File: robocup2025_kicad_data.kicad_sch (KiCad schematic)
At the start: 15 parts, among them M7 Motor_Servo, U2 ESP32-DEVKITC-32E

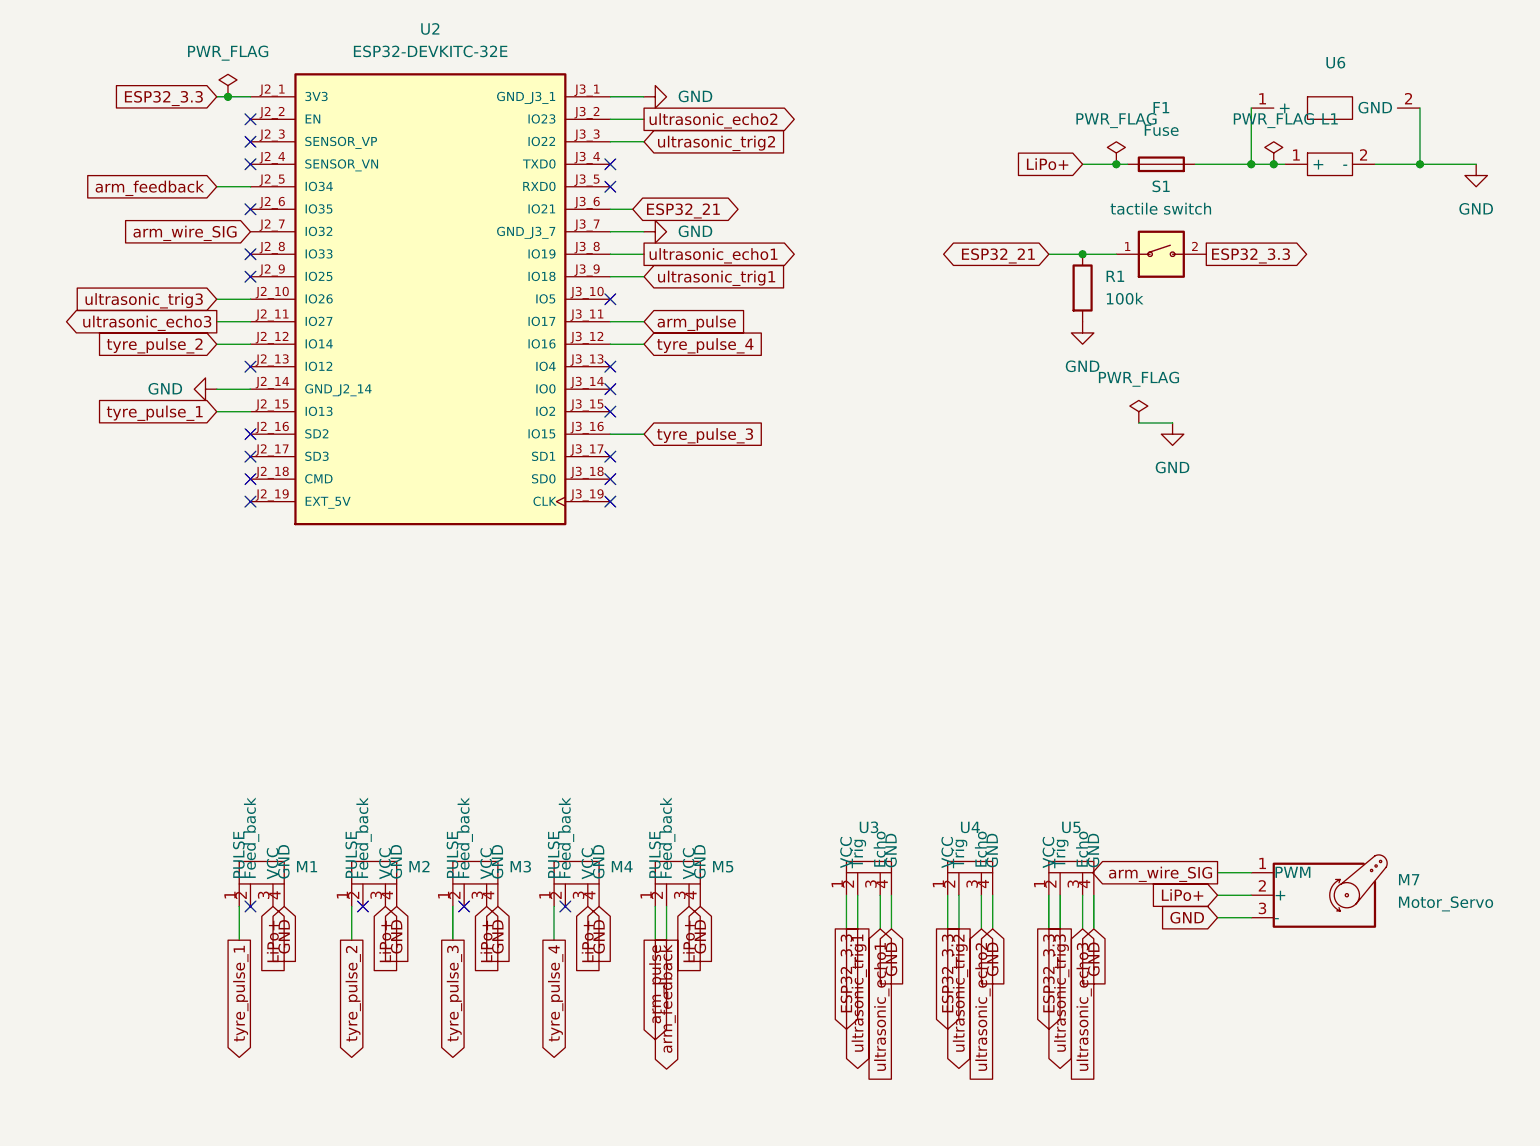
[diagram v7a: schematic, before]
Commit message: Modified pcb's and schematics
Modifying the footprints of the big servo to be able
to connect from pin headers.
Modifying the schematics and pcb's for wire servo
to use 5V instead of LiPo.
Modifying the pcb's lines from 2.0mm to 0.2mm.
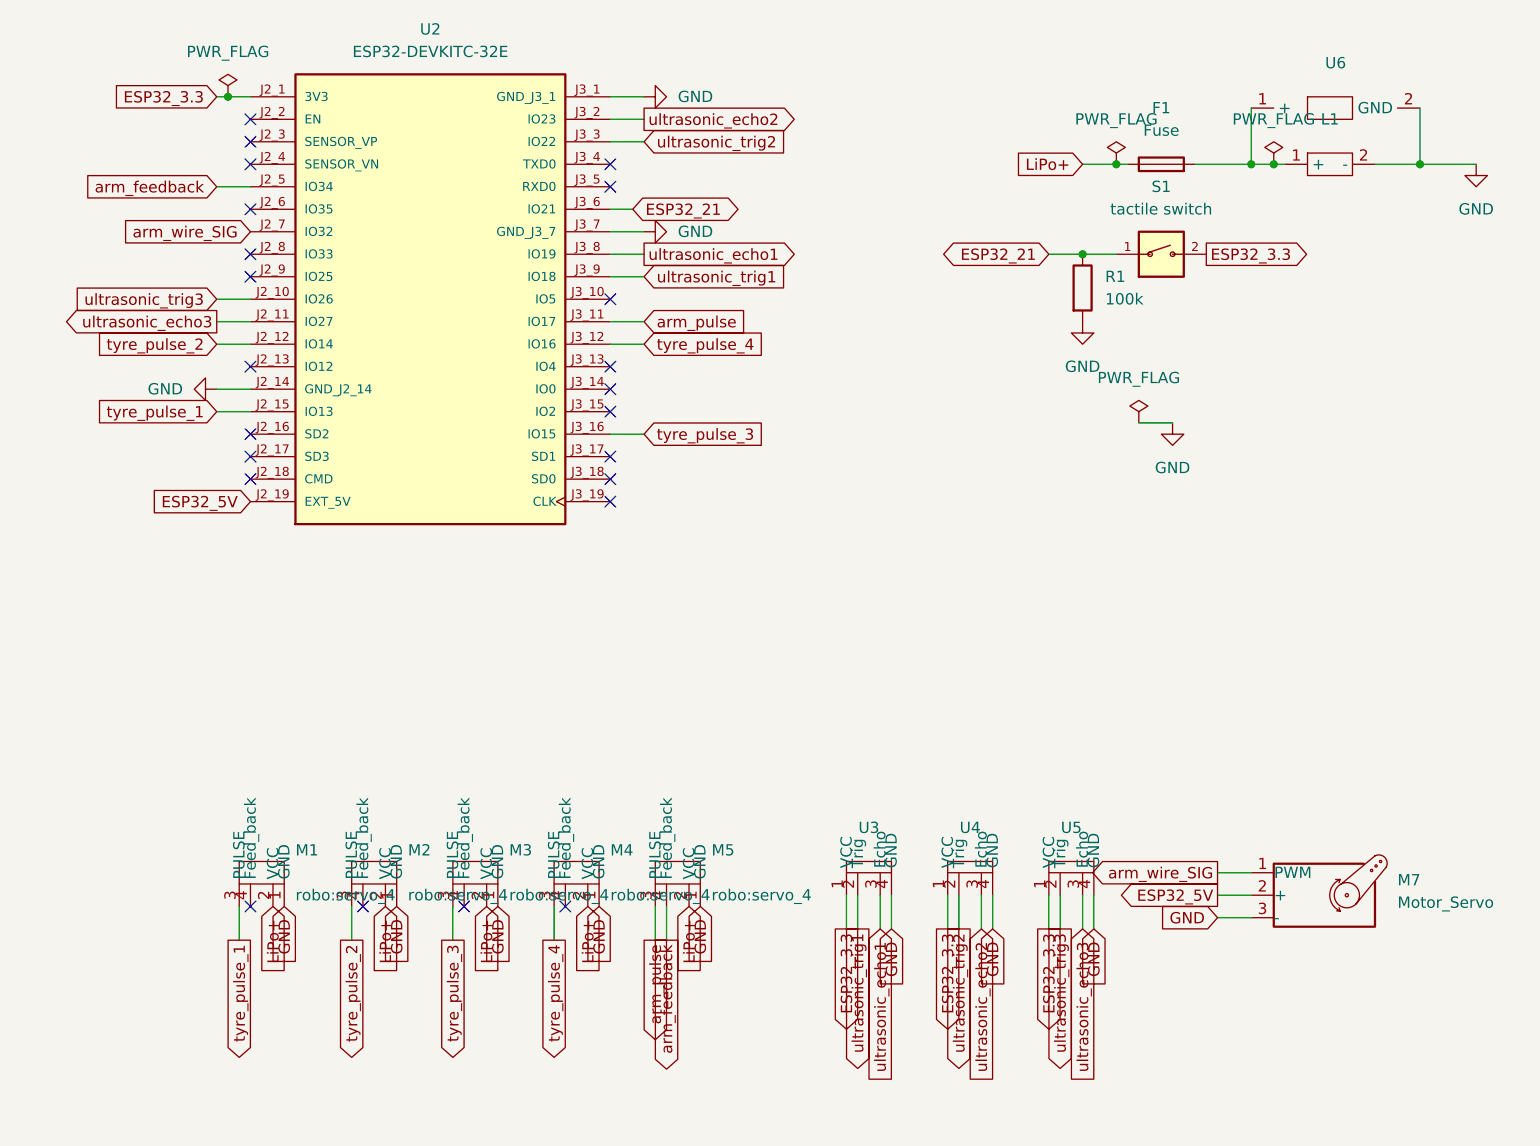
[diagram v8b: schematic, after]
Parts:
- M1, M2, M3, M4, M5: footprint robo:servo_motor_4 -> robo:servo_4
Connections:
- net GND: now also M1.1 (GND), M2.1 (GND), M3.1 (GND), M4.1 (GND), M5.1 (GND); no longer M1.4 (GND), M2.4 (GND), M3.4 (GND), M4.4 (GND), M5.4 (GND)
- net LiPo+: now also M1.2 (VCC), M2.2 (VCC), M3.2 (VCC), M4.2 (VCC), M5.2 (VCC); no longer M1.3 (VCC), M2.3 (VCC), M3.3 (VCC), M4.3 (VCC), M5.3 (VCC), M7.2 (+)
- net arm_feedback: now also M5.4 (Feed_back); no longer M5.2 (Feed_back)
- net arm_pulse: now also M5.3 (PULSE); no longer M5.1 (PULSE)
- net tyre_pulse_1: now also M1.3 (PULSE); no longer M1.1 (PULSE)
- net tyre_pulse_2: now also M2.3 (PULSE); no longer M2.1 (PULSE)
- net tyre_pulse_3: now also M3.3 (PULSE); no longer M3.1 (PULSE)
- net tyre_pulse_4: now also M4.3 (PULSE); no longer M4.1 (PULSE)
- net ESP32_5V: now reaches U2.J2_19 (EXT_5V)
- net ESP32_5V: now also M7.2 (+)
- no-connect marks 24 -> 23
